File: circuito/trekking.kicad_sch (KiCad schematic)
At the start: 30 parts

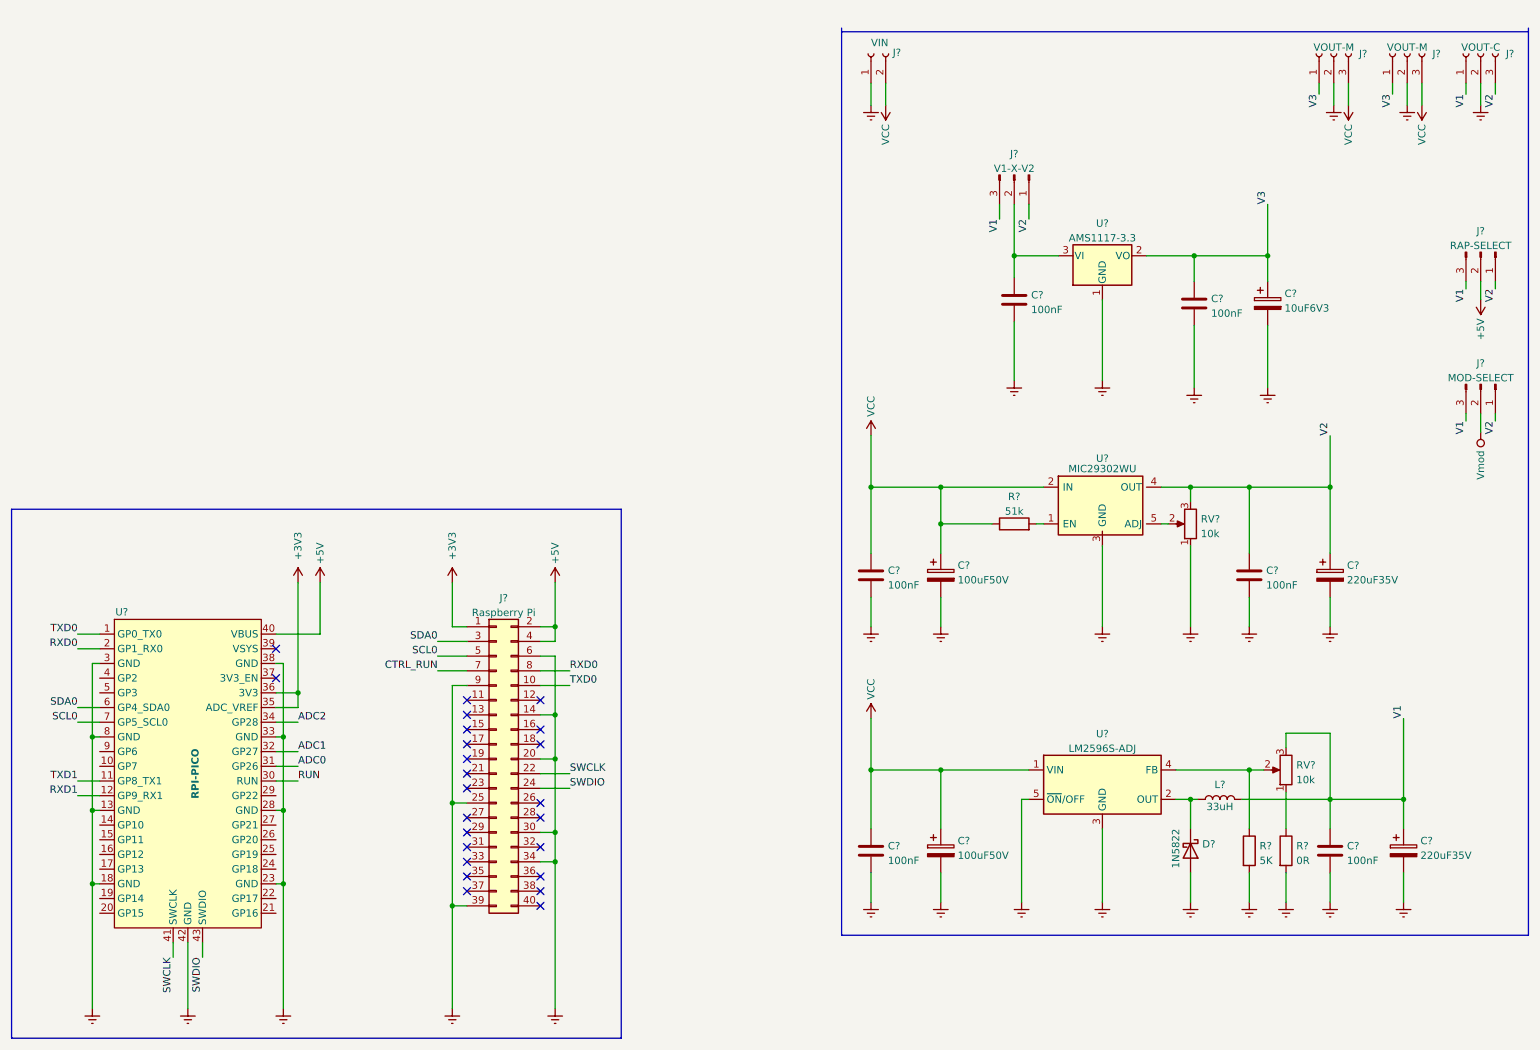
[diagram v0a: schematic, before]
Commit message: cirando circuito
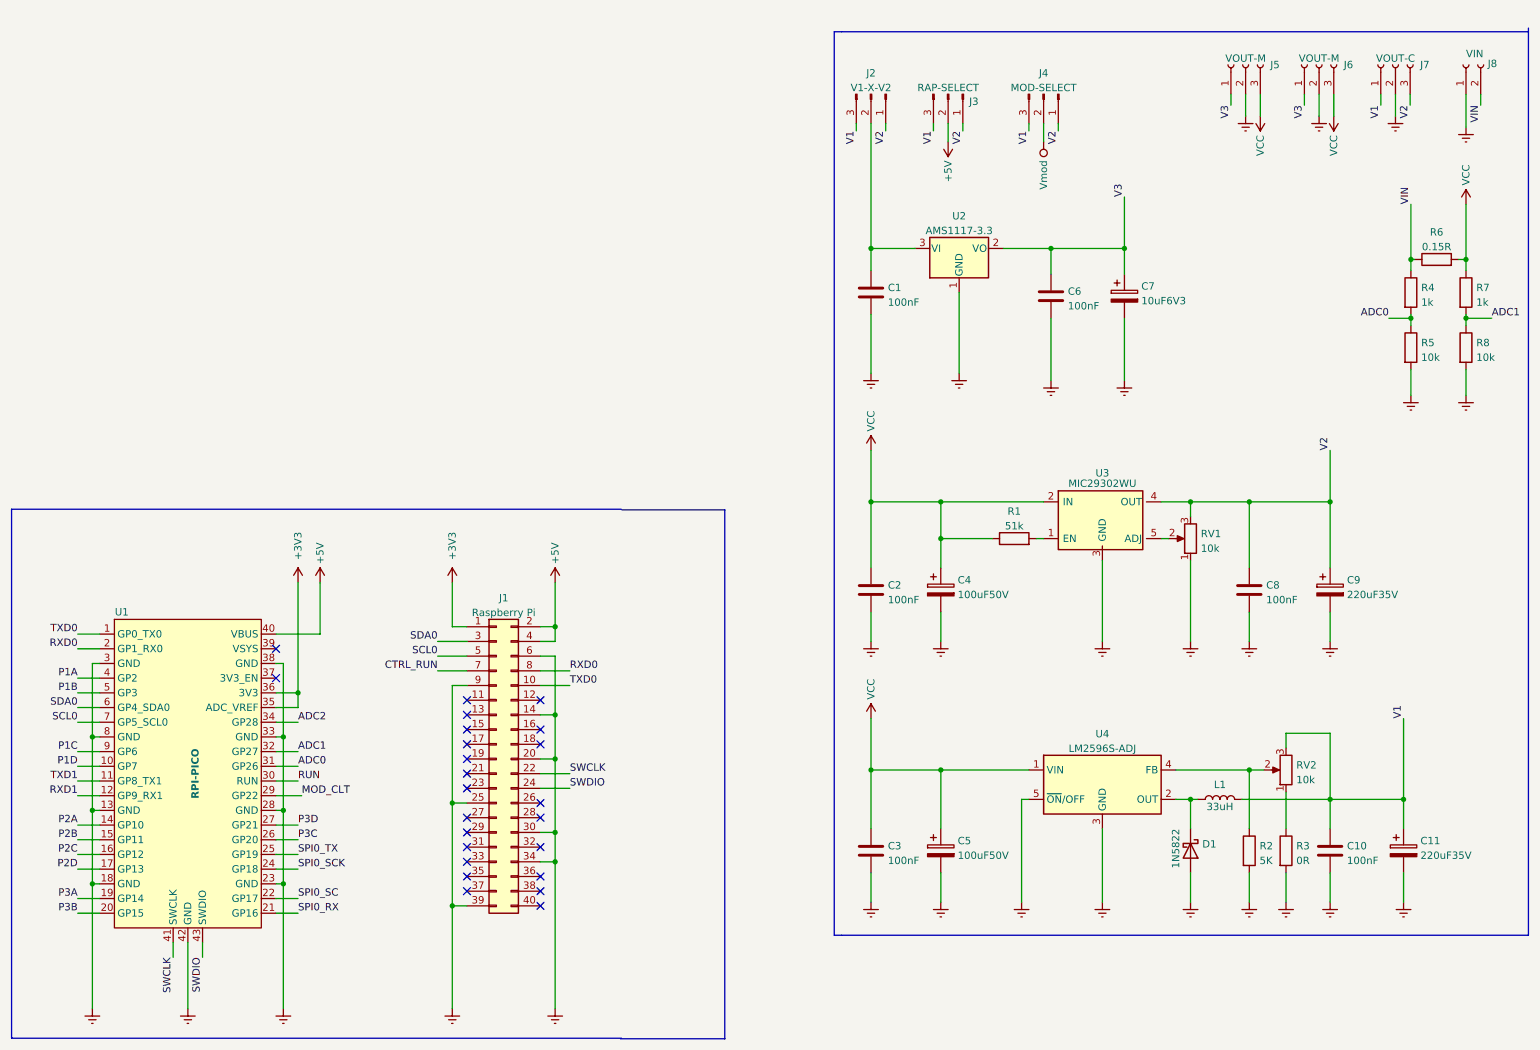
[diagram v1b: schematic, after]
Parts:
- added R4, R7: 1k, Resistor_SMD:R_0805_2012Metric_Pad1.20x1.40mm_HandSolder, symbol Device:R
- added R5, R8: 10k, Resistor_SMD:R_0805_2012Metric_Pad1.20x1.40mm_HandSolder, symbol Device:R
- added R6: 0.15R, symbol Device:R
- C1, C10, C2, C3, C6, C8: renamed from C?; footprint (none) -> Capacitor_SMD:C_0805_2012Metric_Pad1.18x1.45mm_HandSolder
- D1: renamed from D?; footprint Diode_THT:D_DO-201AD_P15.24mm_Horizontal -> Diode_SMD:D_3220_8050Metric_Pad2.65x5.15mm_HandSolder
- J1: renamed from J?; footprint (none) -> Connector_PinHeader_2.54mm:PinHeader_2x20_P2.54mm_Vertical
- J2, J3, J4: renamed from J?; footprint (none) -> Connector_PinHeader_2.54mm:PinHeader_1x03_P2.54mm_Vertical
- J5, J6, J7: renamed from J?; footprint (none) -> MyFootprint:CONN5mm-3
- J8: renamed from J?; footprint (none) -> MyFootprint:AK300-2
- R1, R2, R3: renamed from R?; footprint (none) -> Resistor_SMD:R_0805_2012Metric_Pad1.20x1.40mm_HandSolder
- RV1, RV2: renamed from RV?; footprint (none) -> Potentiometer_THT:Potentiometer_Bourns_3266Y_Vertical
- U3: renamed from U?; footprint TO_SOT_Packages_SMD:TO-252-4 -> Package_TO_SOT_SMD:TO-252-5_TabPin3
- gave numbers to parts that had none: 9
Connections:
- net ADC0: now also R4.2, R5.1
- net ADC1: now also R7.2, R8.1
- net Earth: now also R5.2, R8.2
- net VCC: now also R6.2, R7.1; no longer J8.2 (Pin_2)
- net P1D: now reaches U1.10 (GP7)
- net P2A: now reaches U1.14 (GP10)
- net P2B: now reaches U1.15 (GP11)
- net P2C: now reaches U1.16 (GP12)
- net P2D: now reaches U1.17 (GP13)
- net P3A: now reaches U1.19 (GP14)
- net P3B: now reaches U1.20 (GP15)
- net SPI0_RX: now reaches U1.21 (GP16)
- net SPI0_SC: now reaches U1.22 (GP17)
- net SPI0_SCK: now reaches U1.24 (GP18)
- net SPI0_TX: now reaches U1.25 (GP19)
- net P3C: now reaches U1.26 (GP20)
- net P3D: now reaches U1.27 (GP21)
- net MOD_CLT: now reaches U1.29 (GP22)
- net P1A: now reaches U1.4 (GP2)
- net P1B: now reaches U1.5 (GP3)
- net P1C: now reaches U1.9 (GP6)
- new net VIN: J8.2 (Pin_2), R4.1, R6.1
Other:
- moved on the sheet: C1, C2, C4, C6, C7, C8, C9, J2, J3, J4, J5, J6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

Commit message: cirando circuito
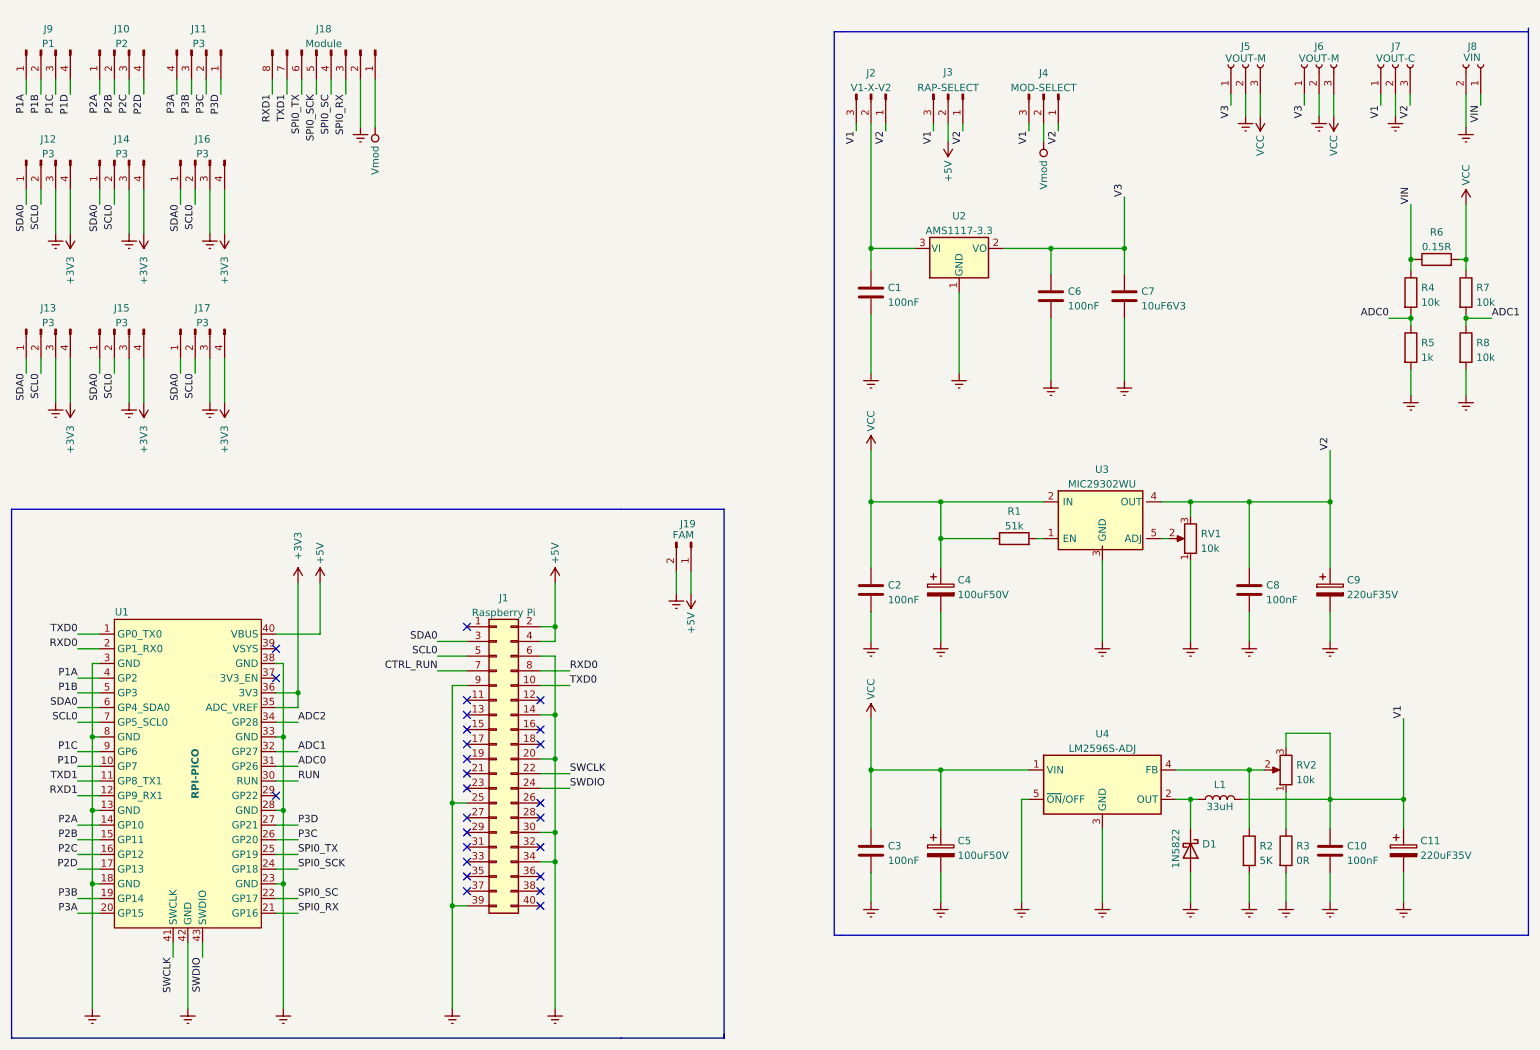
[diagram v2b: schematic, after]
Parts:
- removed C7: 10uF6V3, symbol Device:C_Polarized
- added C7: 10uF6V3, Capacitor_SMD:C_0805_2012Metric_Pad1.18x1.45mm_HandSolder, symbol Device:C
- added J10: P2, Connector_Molex:Molex_KK-254_AE-6410-04A_1x04_P2.54mm_Vertical, symbol Connector:Conn_01x04_Male
- added J11, J12, J13, J14, J15, J16, J17: P3, Connector_Molex:Molex_KK-254_AE-6410-04A_1x04_P2.54mm_Vertical, symbol Connector:Conn_01x04_Male
- added J18: Module, Connector_PinHeader_2.54mm:PinHeader_1x08_P2.54mm_Vertical, symbol Connector:Conn_01x08_Male
- added J19: FAM, Connector_PinHeader_2.54mm:PinHeader_1x02_P2.54mm_Vertical, symbol Connector:Conn_01x02_Male
- added J9: P1, Connector_Molex:Molex_KK-254_AE-6410-04A_1x04_P2.54mm_Vertical, symbol Connector:Conn_01x04_Male
- C1: footprint Capacitor_SMD:C_0805_2012Metric_Pad1.18x1.45mm_HandSolder -> (none)
- C11, C4, C5, C9: footprint (none) -> Capacitor_SMD:CP_Elec_8x10
- L1: footprint (none) -> Inductor_SMD:L_12x12mm_H8mm
- R4, R7: value 1k -> 10k
- R5: value 10k -> 1k
- R6: footprint (none) -> MyFootprint:R_2512_6332Metric_Pad1.40x3.35mm_HandSolder
- U1: footprint (none) -> MyFootprint:RPI-PICO-SMD
- U3: footprint Package_TO_SOT_SMD:TO-252-5_TabPin3 -> Package_TO_SOT_SMD:TO-263-5_TabPin3
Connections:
- net +3V3: now also J12.4 (Pin_4), J13.4 (Pin_4), J14.4 (Pin_4), J15.4 (Pin_4), J16.4 (Pin_4), J17.4 (Pin_4); no longer J1.1 (Pin_1)
- net +5V: now also J19.1 (Pin_1)
- net Earth: now also J8.2 (Pin_2), C7.2, J12.3 (Pin_3), J13.3 (Pin_3), J14.3 (Pin_3), J15.3 (Pin_3), J16.3 (Pin_3), J17.3 (Pin_3), J18.2 (Pin_2), J19.2 (Pin_2); no longer J8.1 (Pin_1)
- net P1A: now also J9.1 (Pin_1)
- net P1B: now also J9.2 (Pin_2)
- net P1C: now also J9.3 (Pin_3)
- net P1D: now also J9.4 (Pin_4)
- net P2A: now also J10.1 (Pin_1)
- net P2B: now also J10.2 (Pin_2)
- net P2C: now also J10.3 (Pin_3)
- net P2D: now also J10.4 (Pin_4)
- net P3A: now also U1.20 (GP15), J11.4 (Pin_4); no longer U1.19 (GP14)
- net P3B: now also U1.19 (GP14), J11.3 (Pin_3); no longer U1.20 (GP15)
- net P3C: now also J11.2 (Pin_2)
- net P3D: now also J11.1 (Pin_1)
- net RXD1: now also J18.8 (Pin_8)
- net SCL0: now also J12.2 (Pin_2), J13.2 (Pin_2), J14.2 (Pin_2), J15.2 (Pin_2), J16.2 (Pin_2), J17.2 (Pin_2)
- net SDA0: now also J12.1 (Pin_1), J13.1 (Pin_1), J14.1 (Pin_1), J15.1 (Pin_1), J16.1 (Pin_1), J17.1 (Pin_1)
- net SPI0_RX: now also J18.3 (Pin_3)
- net SPI0_SC: now also J18.4 (Pin_4)
- net SPI0_SCK: now also J18.5 (Pin_5)
- net SPI0_TX: now also J18.6 (Pin_6)
- net TXD1: now also J18.7 (Pin_7)
- net V3: now also C7.1
- net VIN: now also J8.1 (Pin_1); no longer J8.2 (Pin_2)
- net Vmod: now also J18.1 (Pin_1)
- net MOD_CLT: no longer names the net of U1.29 (GP22)
- no-connect marks 24 -> 26
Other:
- moved on the sheet: J8

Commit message: circuiro rev 1.0
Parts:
- J12, J13, J14, J15, J16, J17: value P3 -> I2C0
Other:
- note added: "CONTROLE"
- note added: "FONTE V1 V2 V3"
- note added: "M2M"
- moved on the sheet: J10, J11, J12, J13, J14, J15, J16, J17, J18, J9

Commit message: circuiro rev 1.0 correção
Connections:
- net SWDIO: now also J1.18 (Pin_18); no longer J1.24 (Pin_24)
- net ADC2: no longer names the net of U1.34 (GP28)
- net CTRL_RUN: no longer names the net of J1.7 (Pin_7)
- net RUN: no longer names the net of U1.30 (RUN)
- no-connect marks 26 -> 29
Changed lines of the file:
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@@
   (no_connect (at 62.865 125.095))
   (no_connect (at 62.865 130.175))
+  (no_connect (at 62.865 137.795))
+  (no_connect (at 62.865 147.955))
+  (no_connect (at 95.885 128.905))
   (no_connect (at 95.885 121.285))
+  (no_connect (at 108.585 149.225))
   (no_connect (at 108.585 154.305))
   (no_connect (at 95.885 154.305))
@@
   (no_connect (at 95.885 146.685))
   (no_connect (at 95.885 149.225))
-  (no_connect (at 108.585 141.605))
   (no_connect (at 108.585 133.985))
   (no_connect (at 95.885 139.065))
@@
     (stroke (width 0) (type default) (color 0 0 0 0))
   )
+  (wire (pts (xy 113.665 141.605) (xy 108.585 141.605))
+    (stroke (width 0) (type default) (color 0 0 0 0))
+  )
   (wire (pts (xy 165.735 55.88) (xy 173.355 55.88))
     (stroke (width 0) (type default) (color 0 0 0 0))
@@
     (stroke (width 0) (type default) (color 0 0 0 0))
   )
-  (wire (pts (xy 108.585 149.225) (xy 113.665 149.225))
-    (stroke (width 0) (type default) (color 0 0 0 0))
-  )
   (wire (pts (xy 28.575 135.255) (xy 32.385 135.255))
     (stroke (width 0) (type default) (color 0 0 0 0))
@@
     (stroke (width 0) (type default) (color 0 0 0 0))
   )
-  (wire (pts (xy 62.865 147.955) (xy 66.675 147.955))
-    (stroke (width 0) (type default) (color 0 0 0 0))
-  )
   (wire (pts (xy 209.55 60.325) (xy 209.55 55.88))
     (stroke (width 0) (type default) (color 0 0 0 0))
@@
   )
   (wire (pts (xy 237.49 163.83) (xy 237.49 168.91))
-    (stroke (width 0) (type default) (color 0 0 0 0))
-  )
-  (wire (pts (xy 90.805 128.905) (xy 95.885 128.905))
-    (stroke (width 0) (type default) (color 0 0 0 0))
-  )
-  (wire (pts (xy 62.865 137.795) (xy 66.675 137.795))
     (stroke (width 0) (type default) (color 0 0 0 0))
   )
@@
     (effects (font (size 1.27 1.27)) (justify right bottom))
   )
-  (label "ADC2" (at 66.675 137.795 0)
-    (effects (font (size 1.27 1.27)) (justify left bottom))
-  )
   (label "P1B" (at 28.575 132.715 180)
     (effects (font (size 1.27 1.27)) (justify right bottom))
@@
     (effects (font (size 1.27 1.27)) (justify right bottom))
   )
-  (label "CTRL_RUN" (at 90.805 128.905 180)
-    (effects (font (size 1.27 1.27)) (justify right bottom))
-  )
   (label "V3" (at 209.55 46.99 90)
     (effects (font (size 1.27 1.27)) (justify left bottom))
@@
     (effects (font (size 1.27 1.27)) (justify right bottom))
   )
-  (label "RUN" (at 66.675 147.955 0)
-    (effects (font (size 1.27 1.27)) (justify left bottom))
-  )
   (label "V1" (at 193.04 35.56 270)
     (effects (font (size 1.27 1.27)) (justify right bottom))
@@
     (effects (font (size 1.27 1.27)) (justify right bottom))
   )
-  (label "SWDIO" (at 113.665 149.225 0)
-    (effects (font (size 1.27 1.27)) (justify left bottom))
-  )
+  (label "SWDIO" (at 113.665 141.605 0)
+    (effects (font (size 1.27 1.27)) (justify left bottom))
+  )
